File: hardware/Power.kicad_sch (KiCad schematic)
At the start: 18 parts, among them J201 4090 USB-C, J202 9V battery, U201 LM1117T-5.0

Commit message: Add final planned components
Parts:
- added D204: Red LED, LED_THT:LED_D5.0mm, symbol Device:LED
- added R201: 100k, Resistor_THT:R_Axial_DIN0207_L6.3mm_D2.5mm_P7.62mm_Horizontal, symbol Device:R
- added R202: 47k, Resistor_THT:R_Axial_DIN0207_L6.3mm_D2.5mm_P7.62mm_Horizontal, symbol Device:R
- added R203: 330, Resistor_THT:R_Axial_DIN0207_L6.3mm_D2.5mm_P7.62mm_Horizontal, symbol Device:R
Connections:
- net GND: now also D204.1 (K), R202.2
- net at C203.1, J202.2 (Pin_2), U201.3 (VI): now also R201.1
- net at C201.1, C202.2, D201.2 (A)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: now also R203.2
- new net: D204.2 (A), R203.1
- new net ~{BATLOW}: R201.2, R202.1
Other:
- note added: "Potential divider for low battery level sense (threshold voltage is ~6.5 V)"
- moved on the sheet: C203, C204, C205, C206, C207, C208, C209, C210, C211, C212, D201, D202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

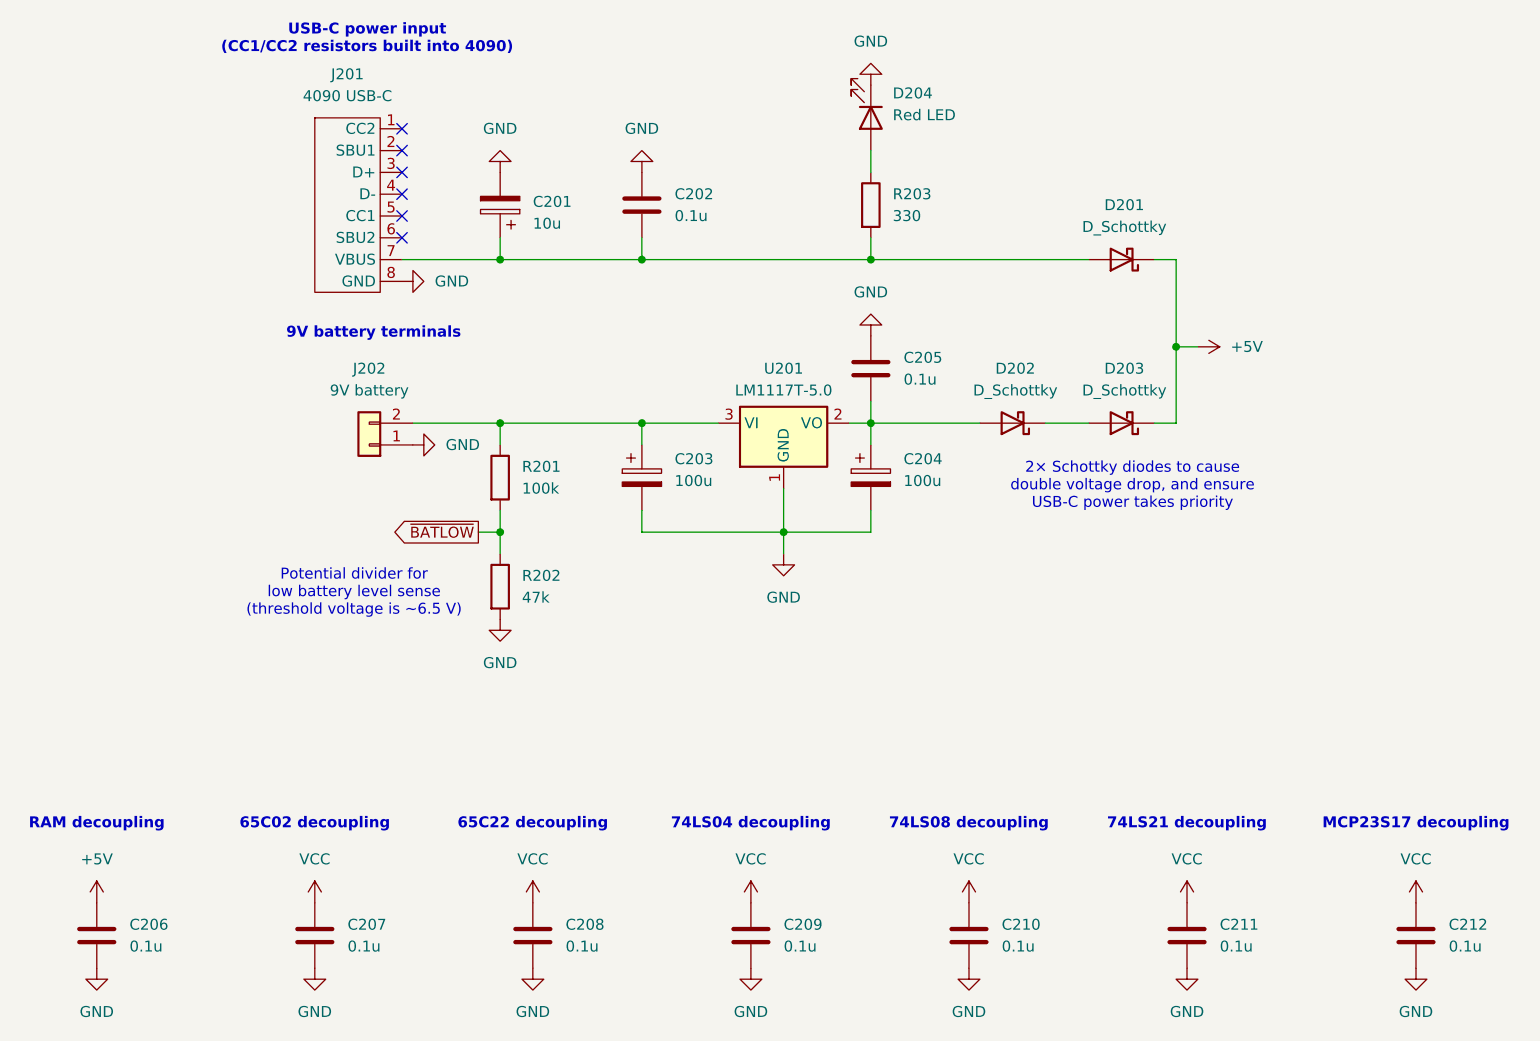
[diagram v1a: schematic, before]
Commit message: Modify power circuitry to use better diode arrangement and more energy-efficient regulator
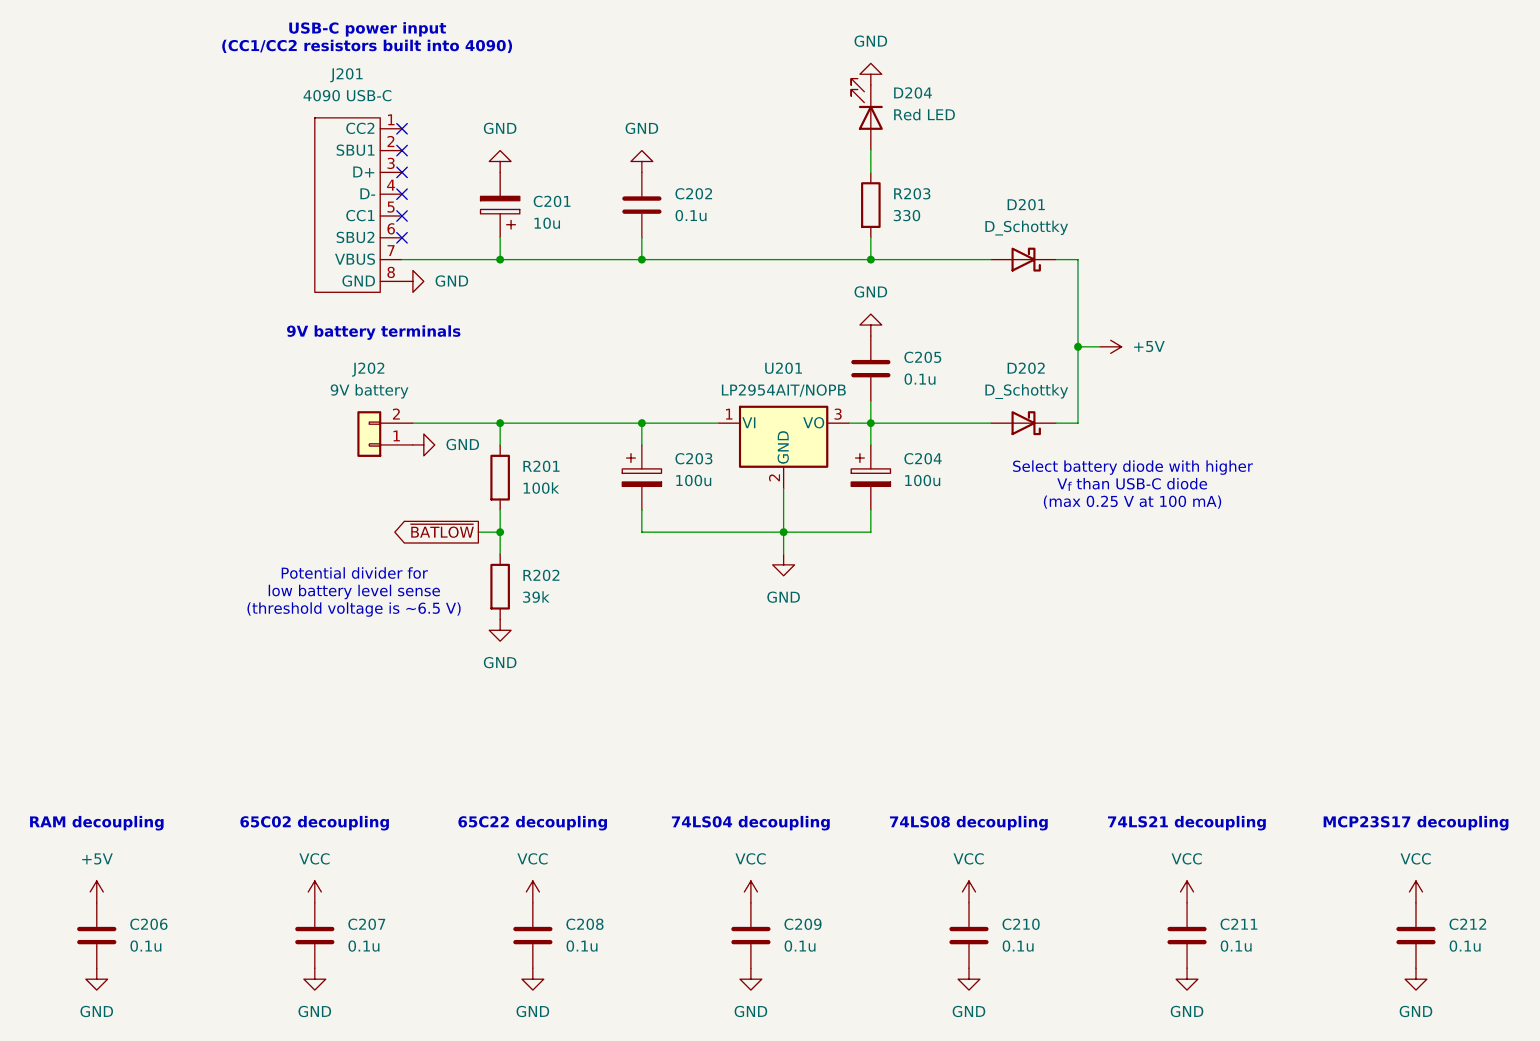
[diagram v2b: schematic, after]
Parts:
- removed D203: D_Schottky, Diode_THT:D_DO-41_SOD81_P7.62mm_Horizontal, symbol Device:D_Schottky
- removed U201: LM1117T-5.0, Package_TO_SOT_THT:TO-220-3_Horizontal_TabDown, symbol Regulator_Linear:LM1117T-5.0
- added U201: LP2954AIT/NOPB, Package_TO_SOT_THT:TO-220-3_Vertical, symbol Regulator_Linear:LF50_TO220
- C205, C206, C207, C208, C209, C210, C211, C212: footprint Capacitor_THT:CP_Radial_D4.0mm_P1.50mm -> Capacitor_THT:C_Radial_D4.0mm_H5.0mm_P1.50mm
- R202: value 47k -> 39k
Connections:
- net +5V: now also D202.1 (K)
- net GND: now also U201.2 (GND)
- net at C203.1, J202.2 (Pin_2), R201.1: now also U201.1 (VI)
- net at C204.1, C205.2, D202.2 (A): now also U201.3 (VO)
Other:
- note added: "Select battery diode with higher V_{f} than USB-C diode (max 0.25 V at 100 mA)"
- note removed: "2× Schottky diodes to cause double voltage drop, and ensure USB-C power takes priority"
- moved on the sheet: D201, D202
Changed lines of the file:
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@@
 		)
 	)
-	(text "2× Schottky diodes to cause\ndouble voltage drop, and ensure\nUSB-C power takes priority"
+	(text "Select battery diode with higher\nV_{f} than USB-C diode\n(max 0.25 V at 100 mA)"
 		(exclude_from_sim no)
 		(at 196.85 87.376 0)
@@
 	)
 	(junction
-		(at 201.93 71.12)
+		(at 190.5 71.12)
 		(diameter 0)
 		(color 0 0 0 0)
@@
 	(wire
 		(pts
-			(xy 186.69 80.01) (xy 191.77 80.01)
-		)
-		(stroke
-			(width 0)
-			(type default)
-		)
-	)
-	(wire
-		(pts
 			(xy 139.7 60.96) (xy 166.37 60.96)
 		)
@@
 	(wire
 		(pts
-			(xy 201.93 60.96) (xy 201.93 71.12)
+			(xy 190.5 60.96) (xy 190.5 71.12)
 		)
 		(stroke
@@
 	(wire
 		(pts
-			(xy 199.39 60.96) (xy 201.93 60.96)
+			(xy 187.96 60.96) (xy 190.5 60.96)
 		)
 		(stroke
@@
 	(wire
 		(pts
-			(xy 201.93 71.12) (xy 204.47 71.12)
+			(xy 190.5 71.12) (xy 193.04 71.12)
 		)
 		(stroke
@@
 	(wire
 		(pts
-			(xy 166.37 80.01) (xy 179.07 80.01)
+			(xy 166.37 80.01) (xy 180.34 80.01)
 		)
 		(stroke
@@
 	(wire
 		(pts
-			(xy 201.93 71.12) (xy 201.93 80.01)
+			(xy 190.5 71.12) (xy 190.5 80.01)
 		)
 		(stroke
@@
 	(wire
 		(pts
-			(xy 166.37 60.96) (xy 191.77 60.96)
+			(xy 166.37 60.96) (xy 180.34 60.96)
 		)
 		(stroke
@@
 	(wire
 		(pts
-			(xy 201.93 80.01) (xy 199.39 80.01)
+			(xy 190.5 80.01) (xy 187.96 80.01)
 		)
 		(stroke
@@
 			)
 		)
-		(property "Footprint" "Capacitor_THT:CP_Radial_D4.0mm_P1.50mm"
+		(property "Footprint" "Capacitor_THT:C_Radial_D4.0mm_H5.0mm_P1.50mm"
 			(at 77.1652 143.51 0)
 			(effects
@@
 	(symbol
 		(lib_id "Device:D_Schottky")
-		(at 195.58 60.96 180)
+		(at 184.15 60.96 180)
 		(unit 1)
 		(exclude_from_sim no)
@@
 		(fields_autoplaced yes)
 		(property "Reference" "D201"
-			(at 195.8975 54.61 0)
+			(at 184.4675 54.61 0)
 			(effects
 				(font
@@
 		)
 		(property "Value" "D_Schottky"
-			(at 195.8975 57.15 0)
+			(at 184.4675 57.15 0)
 			(effects
 				(font
@@
 		)
 		(property "Footprint" "Diode_THT:D_DO-41_SOD81_P7.62mm_Horizontal"
-			(at 195.58 60.96 0)
+			(at 184.15 60.96 0)
 			(effects
 				(font
@@
 		)
 		(property "Datasheet" "~"
-			(at 195.58 60.96 0)
+			(at 184.15 60.96 0)
 			(effects
 				(font
@@
 		)
 		(property "Description" "Schottky diode"
-			(at 195.58 60.96 0)
+			(at 184.15 60.96 0)
 			(effects
 				(font
@@
 	)
 	(symbol
-		(lib_id "Device:D_Schottky")
-		(at 195.58 80.01 180)
-		(unit 1)
-		(exclude_from_sim no)
-		(in_bom yes)
-		(on_board yes)
-		(dnp no)
-		(fields_autoplaced yes)
-		(property "Reference" "D203"
-			(at 195.8975 73.66 0)
-			(effects
-				(font
-					(size 1.27 1.27)
-				)
-			)
-		)
-		(property "Value" "D_Schottky"
-			(at 195.8975 76.2 0)
-			(effects
-				(font
-					(size 1.27 1.27)
-				)
-			)
-		)
-		(property "Footprint" "Diode_THT:D_DO-41_SOD81_P7.62mm_Horizontal"
-			(at 195.58 80.01 0)
-			(effects
-				(font
-					(size 1.27 1.27)
-				)
-				(hide yes)
-			)
-		)
-		(property "Datasheet" "~"
-			(at 195.58 80.01 0)
-			(effects
-				(font
-					(size 1.27 1.27)
-				)
-				(hide yes)
-			)
-		)
-		(property "Description" "Schottky diode"
-			(at 195.58 80.01 0)
-			(effects
-				(font
-					(size 1.27 1.27)
-				)
-				(hide yes)
-			)
-		)
-		(pin "2"
-		)
-		(pin "1"
-		)
-		(instances
-			(project "FCom-8"
-				(path "/d870bcaf-2f1b-46ce-b0b4-300d405a54b8/5b699d3c-84a6-4a70-ac7d-020a173c82b3"
-					(reference "D203")
-					(unit 1)
-				)
-			)
-		)
-	)
-	(symbol
 		(lib_id "power:+5V")
-		(at 204.47 71.12 270)
+		(at 193.04 71.12 270)
 		(unit 1)
 		(exclude_from_sim no)
@@
 		(fields_autoplaced yes)
 		(property "Reference" "#PWR0204"
-			(at 200.66 71.12 0)
+			(at 189.23 71.12 0)
 			(effects
 				(font
@@
 		)
 		(property "Value" "+5V"
-			(at 208.28 71.1199 90)
+			(at 196.85 71.1199 90)
 			(effects
 				(font
@@
 		)
 		(property "Footprint" ""
-			(at 204.47 71.12 0)
+			(at 193.04 71.12 0)
 			(effects
 				(font
@@
 		)
 		(property "Datasheet" ""
-			(at 204.47 71.12 0)
+			(at 193.04 71.12 0)
 			(effects
 				(font
@@
 		)
 		(property "Description" "Power symbol creates a global label with name \"+5V\""
-			(at 204.47 71.12 0)
+			(at 193.04 71.12 0)
 			(effects
 				(font
@@
 			)
 		)
-		(property "Footprint" "Capacitor_THT:CP_Radial_D4.0mm_P1.50mm"
+		(property "Footprint" "Capacitor_THT:C_Radial_D4.0mm_H5.0mm_P1.50mm"
 			(at 204.1652 143.51 0)
 			(effects
@@
 			)
 		)
-		(property "Footprint" "Capacitor_THT:CP_Radial_D4.0mm_P1.50mm"
+		(property "Footprint" "Capacitor_THT:C_Radial_D4.0mm_H5.0mm_P1.50mm"
 			(at 102.5652 143.51 0)
 			(effects
@@
 			)
 		)
-		(property "Footprint" "Capacitor_THT:CP_Radial_D4.0mm_P1.50mm"
+		(property "Footprint" "Capacitor_THT:C_Radial_D4.0mm_H5.0mm_P1.50mm"
 			(at 230.8352 143.51 0)
 			(effects
@@
 	)
 	(symbol
-		(lib_id "Regulator_Linear:LM1117T-5.0")
-		(at 156.21 80.01 0)
-		(unit 1)
-		(exclude_from_sim no)
-		(in_bom yes)
-		(on_board yes)
-		(dnp no)
-		(fields_autoplaced yes)
-		(property "Reference" "U201"
-			(at 156.21 73.66 0)
-			(effects
-				(font
-					(size 1.27 1.27)
-				)
-			)
-		)
-		(property "Value" "LM1117T-5.0"
-			(at 156.21 76.2 0)
-			(effects
-				(font
-					(size 1.27 1.27)
-				)
-			)
-		)
-		(property "Footprint" "Package_TO_SOT_THT:TO-220-3_Horizontal_TabDown"
-			(at 156.21 80.01 0)
-			(effects
-				(font
-					(size 1.27 1.27)
-				)
-				(hide yes)
-			)
-		)
-		(property "Datasheet" "http://www.ti.com/lit/ds/symlink/lm1117.pdf"
-			(at 156.21 80.01 0)
-			(effects
-				(font
-					(size 1.27 1.27)
-				)
-				(hide yes)
-			)
-		)
-		(property "Description" "800mA Low-Dropout Linear Regulator, 5.0V fixed output, TO-220"
-			(at 156.21 80.01 0)
-			(effects
-				(font
-					(size 1.27 1.27)
-				)
-				(hide yes)
-			)
-		)
-		(pin "2"
-		)
-		(pin "1"
-		)
-		(pin "3"
-		)
-		(instances
-			(project ""
-				(path "/d870bcaf-2f1b-46ce-b0b4-300d405a54b8/5b699d3c-84a6-4a70-ac7d-020a173c82b3"
-					(reference "U201")
-					(unit 1)
-				)
-			)
-		)
-	)
-	(symbol
 		(lib_id "Device:C")
 		(at 152.4 139.7 0)
@@
 			)
 		)
-		(property "Footprint" "Capacitor_THT:CP_Radial_D4.0mm_P1.50mm"
+		(property "Footprint" "Capacitor_THT:C_Radial_D4.0mm_H5.0mm_P1.50mm"
 			(at 153.3652 143.51 0)
 			(effects
@@
 			)
 		)
-		(property "Value" "47k"
+		(property "Value" "39k"
 			(at 125.73 100.3299 0)
 			(effects
@@
 	(symbol
 		(lib_id "Device:D_Schottky")
-		(at 182.88 80.01 180)
+		(at 184.15 80.01 180)
 		(unit 1)
 		(exclude_from_sim no)
@@
 		(fields_autoplaced yes)
 		(property "Reference" "D202"
-			(at 183.1975 73.66 0)
+			(at 184.4675 73.66 0)
 			(effects
 				(font
@@
 		)
 		(property "Value" "D_Schottky"
-			(at 183.1975 76.2 0)
+			(at 184.4675 76.2 0)
 			(effects
 				(font
@@
 		)
 		(property "Footprint" "Diode_THT:D_DO-41_SOD81_P7.62mm_Horizontal"
-			(at 182.88 80.01 0)
+			(at 184.15 80.01 0)
 			(effects
 				(font
@@
 		)
 		(property "Datasheet" "~"
-			(at 182.88 80.01 0)
+			(at 184.15 80.01 0)
 			(effects
 				(font
@@
 		)
 		(property "Description" "Schottky diode"
-			(at 182.88 80.01 0)
+			(at 184.15 80.01 0)
 			(effects
 				(font
@@
 			)
 		)
-		(property "Footprint" "Capacitor_THT:CP_Radial_D4.0mm_P1.50mm"
+		(property "Footprint" "Capacitor_THT:C_Radial_D4.0mm_H5.0mm_P1.50mm"
 			(at 127.9652 143.51 0)
 			(effects
@@
 			)
 		)
-		(property "Footprint" "Capacitor_THT:CP_Radial_D4.0mm_P1.50mm"
+		(property "Footprint" "Capacitor_THT:C_Radial_D4.0mm_H5.0mm_P1.50mm"
 			(at 167.3352 77.47 0)
 			(effects
@@
 			)
 		)
-		(property "Footprint" "Capacitor_THT:CP_Radial_D4.0mm_P1.50mm"
+		(property "Footprint" "Capacitor_THT:C_Radial_D4.0mm_H5.0mm_P1.50mm"
 			(at 178.7652 143.51 0)
 			(effects
@@
 					(unit 1)
 				)
+			)
+		)
+	)
+	(symbol
+		(lib_id "Regulator_Linear:LF50_TO220")
+		(at 156.21 80.01 0)
+		(unit 1)
+		(exclude_from_sim no)
+		(in_bom yes)
+		(on_board yes)
+		(dnp no)
+		(fields_autoplaced yes)
+		(property "Reference" "U201"
+			(at 156.21 73.66 0)
+			(effects
+				(font
+					(size 1.27 1.27)
+				)
+			)
+		)
+		(property "Value" "LP2954AIT/NOPB"
+			(at 156.21 76.2 0)
+			(effects
+				(font
+					(size 1.27 1.27)
+				)
+			)
+		)
+		(property "Footprint" "Package_TO_SOT_THT:TO-220-3_Vertical"
+			(at 156.21 74.295 0)
+			(effects
+				(font
+					(size 1.27 1.27)
+					(italic yes)
+				)
+				(hide yes)
+			)
+		)
+		(property "Datasheet" "http://www.st.com/content/ccc/resource/technical/document/datasheet/c4/0e/7e/2a/be/bc/4c/bd/CD00000546.pdf/files/CD00000546.pdf/jcr:content/translations/en.CD00000546.pdf"
+			(at 156.21 81.28 0)
+			(effects
+				(font
+					(size 1.27 1.27)
+				)
+				(hide yes)
+			)
+		)
+		(property "Description" "Low-drop Voltage Regulator, Io up to 500mA, Fixed Vo 5.0V, TO-220"
+			(at 156.21 80.01 0)
+			(effects
+				(font
+					(size 1.27 1.27)
+				)
+				(hide yes)
+			)
+		)
+		(pin "2"
+		)
+		(pin "1"
+		)
+		(pin "3"
+		)
+		(instances
+			(project ""
+				(path "/d870bcaf-2f1b-46ce-b0b4-300d405a54b8/5b699d3c-84a6-4a70-ac7d-020a173c82b3"
+					(reference "U201")
+					(unit 1)
+				)
